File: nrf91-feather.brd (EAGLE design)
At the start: 50.8 x 22.9 mm, 126 parts, among them J1 CON-USB-1050170001, J2 CON-HEADER-1X12-MALE-PIN, J3 CON-HEADER-1X16-MALE-PIN, J4 CON-1909763-1, J5 CON-SIM-104224-0820, J6 CON-S2B-PH-SM4-TB(LF)(SN), J7 CON-1909763-1, J9 CON-TC2030-MCP-NL, Q1 MOSFET-P-SC89, Q2 MOSFET-DUAL-COMP-SOT563, Q3 MOSFET-P-20V-4.7A-SOT23, Q4 MOSFET-N-SC89, Q5 MOSFET-N-SC89, SW1 SW-EVP-AA402W, SW2 SW-EVP-AA402W, U1 MOD-NRF9160-SICA-R, U10 IC-LIS2DH12TR, U2 IC-CP2102N-A02-GQFN20R, U3 IC-TPS63031DSKR, U5 IC-TPD4S012DRYR, U6 FLASH-W25Q32JVZPIQ-WSON, U7 IC-STBC08PMR, U8 IC-PCF85063ATL/1, U9 IC-BAV70S, Y1 XTAL-ABS07AIG-32.768KHZ-7-T

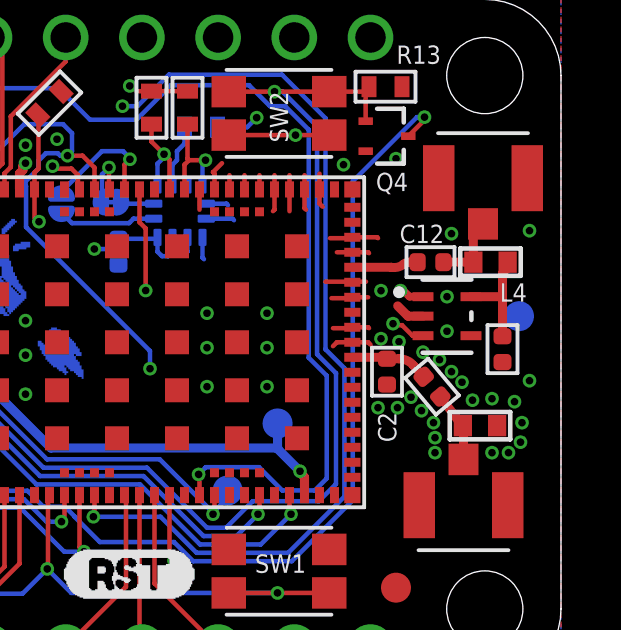
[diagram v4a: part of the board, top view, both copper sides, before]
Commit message: Undo changing U4 to LDO. Needs to stay as a load switch.
Changed:
* U4 back to the original part.
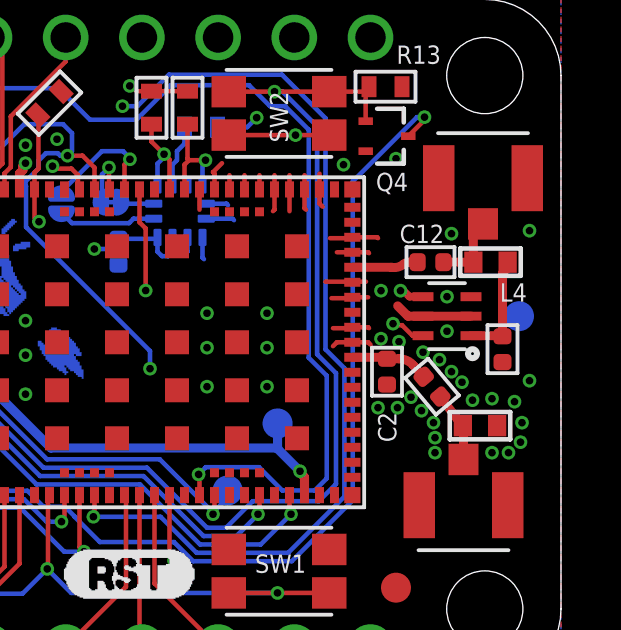
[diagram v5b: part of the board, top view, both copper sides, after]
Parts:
- U4: value (none) -> POWER-SWITCH-MIC94092YC6; device wolff-den:SOT353 -> wolff-den:SOT363
- turned U4 to 90 degrees
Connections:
- net +3V3: now also U4.4; no longer U4.1
- net COEX0/LNA_EN: now also U4.6; no longer U4.3
- net GND: now also U4.5
- net LNA_SW_OUT: now also U4.1; no longer U4.5
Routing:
- net GND: track 47.1 -> 48.7 mm
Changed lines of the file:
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@@
 <layer number="49" name="Reference" color="7" fill="1" visible="no" active="yes"/>
 <layer number="50" name="dxf" color="7" fill="1" visible="no" active="no"/>
-<layer number="51" name="tDocu" color="7" fill="1" visible="yes" active="yes"/>
+<layer number="51" name="tDocu" color="7" fill="1" visible="no" active="yes"/>
 <layer number="52" name="bDocu" color="7" fill="1" visible="no" active="yes"/>
 <layer number="53" name="tGND_GNDA" color="7" fill="9" visible="no" active="no"/>
@@
 <attribute name="TOLERANCE" value="5%" x="5.8" y="5.9" size="1.778" layer="27" display="off"/>
 </element>
-<element name="U4" library="wolff-den" library_urn="urn:adsk.eagle:library:6370453" package="SOT353" package3d_urn="urn:adsk.eagle:package:19061981/1" value="" x="47" y="12.3" smashed="yes">
-<attribute name="DESC" value="IC REG LINEAR 2.8V 150MA SC70-5" x="47" y="12.3" size="1.778" layer="27" display="off"/>
-<attribute name="DIGIKEYPN" value="576-3187-1-ND" x="47" y="12.3" size="1.778" layer="27" display="off"/>
-<attribute name="MPN" value="MIC5365-2.8YC5-TR" x="47" y="12.3" size="1.778" layer="27" display="off"/>
-<attribute name="NAME" x="45.0965" y="11.89428125" size="0.6096" layer="25" font="vector" ratio="20" rot="R90"/>
-<attribute name="NAME" x="47" y="12.3" size="0.2" layer="51" align="center"/>
+<element name="U4" library="wolff-den" library_urn="urn:adsk.eagle:library:6370453" package="SOT363" package3d_urn="urn:adsk.eagle:package:5807345/9" value="POWER-SWITCH-MIC94092YC6" x="47" y="12.3" smashed="yes" rot="R90">
+<attribute name="DESC" value="IC LOAD SW HGH SIDE 1.2A SC70-6" x="47" y="12.3" size="1.778" layer="27" rot="R90" display="off"/>
+<attribute name="DIGIKEYPN" value="576-3488-1-ND" x="47" y="12.3" size="1.778" layer="27" rot="R90" display="off"/>
+<attribute name="MPN" value="MIC94092YC6-TR" x="47" y="12.3" size="1.778" layer="27" rot="R90" display="off"/>
+<attribute name="NAME" x="44.5035" y="12.95571875" size="0.6096" layer="25" font="vector" ratio="20" rot="R270"/>
+<attribute name="NAME" x="47" y="12.3" size="0.2" layer="51" rot="R90" align="center"/>
 </element>
 <element name="C2" library="wolff-den" library_urn="urn:adsk.eagle:library:6370453" package="CAPC1005X55N" package3d_urn="urn:adsk.eagle:package:7419912/5" value="15p" x="45" y="10.45" smashed="yes" rot="R270">
@@
 <wire x1="44.85" y1="13.15" x2="44.8" y2="13.15" width="0.3" layer="1"/>
 <wire x1="45.69950625" y1="12.3" x2="45.35510625" y2="12.6444" width="0.3" layer="1"/>
-<wire x1="46.2" y1="12.3" x2="45.69950625" y2="12.3" width="0.3" layer="1"/>
+<wire x1="47.8" y1="12.3" x2="45.69950625" y2="12.3" width="0.3" layer="1"/>
 <contactref element="U10" pad="7"/>
 <contactref element="U10" pad="6"/>
@@
 <via x="11.8" y="4.45" extent="1-16" drill="0.254"/>
 <via x="12.85" y="4.85" extent="1-16" drill="0.254"/>
+<contactref element="U4" pad="5"/>
 </signal>
 <signal name="+3V3">
@@
 <wire x1="36.45" y1="20" x2="36.425" y2="19.975" width="0.1524" layer="1"/>
 <via x="36.425" y="19.975" extent="1-16" drill="0.254"/>
-<contactref element="U4" pad="1"/>
+<contactref element="U4" pad="4"/>
 <wire x1="45.45" y1="13.15" x2="45.55" y2="13.15" width="0.254" layer="1"/>
 <wire x1="45.75" y1="12.95" x2="45.55" y2="13.15" width="0.254" layer="1"/>
@@
 <wire x1="33.4" y1="15.45" x2="33.8794" y2="14.9706" width="0.1524" layer="2"/>
 <contactref element="R1" pad="2"/>
-<contactref element="U4" pad="3"/>
+<contactref element="U4" pad="6"/>
 <wire x1="46.2" y1="11.65" x2="45.85" y2="11.65" width="0.1524" layer="1"/>
 <wire x1="45.2" y1="12.05" x2="45.1842" y2="12.05" width="0.1524" layer="2"/>
@@
 <contactref element="L4" pad="1"/>
 <contactref element="C19" pad="1"/>
-<contactref element="U4" pad="5"/>
+<contactref element="U4" pad="1"/>
 <wire x1="49.11075" y1="14.01075" x2="49.11075" y2="13.98925" width="0.254" layer="1"/>
-<wire x1="48.85" y1="11.63" x2="48.83" y2="11.65" width="0.3" layer="1"/>
 <wire x1="49.11075" y1="13.98925" x2="48.85" y2="13.7285" width="0.3" layer="1"/>
-<wire x1="48.85" y1="11.63" x2="48.85" y2="12.95" width="0.3" layer="1"/>
-<wire x1="48.85" y1="12.95" x2="48.85" y2="13.7285" width="0.3" layer="1"/>
+<wire x1="48.85" y1="11.63" x2="48.85" y2="13.7285" width="0.3" layer="1"/>
 <wire x1="49.0215" y1="14.1" x2="49.11075" y2="14.01075" width="0.3" layer="1"/>
-<wire x1="47.8" y1="12.95" x2="48.85" y2="12.95" width="0.3" layer="1"/>
+<wire x1="47.8" y1="11.65" x2="48.83" y2="11.65" width="0.3" layer="1"/>
+<wire x1="48.83" y1="11.65" x2="48.85" y2="11.63" width="0.3" layer="1"/>
 </signal>
 <signal name="GPS_ANT" class="2">

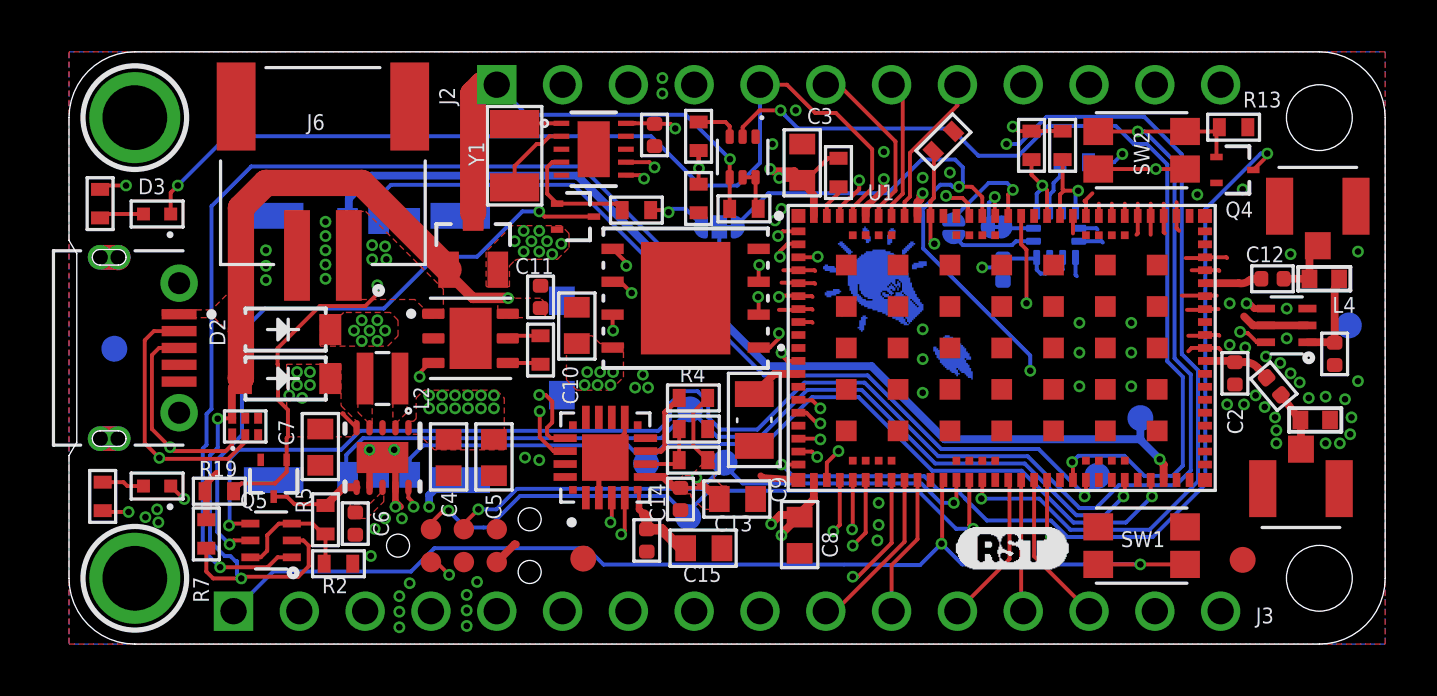
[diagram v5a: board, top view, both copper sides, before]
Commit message: Changes for next revision of the nRF9160 Feather
Removed:
* TVS diode

Changed:
* USB is now USB-C
* Power supply is now Boost + LDO combo (not final)
* LED position due to USB-C being larger
* Changed Schottky diodes to a TSC part
* Re-routed and cleaned up some signals on the inner layer
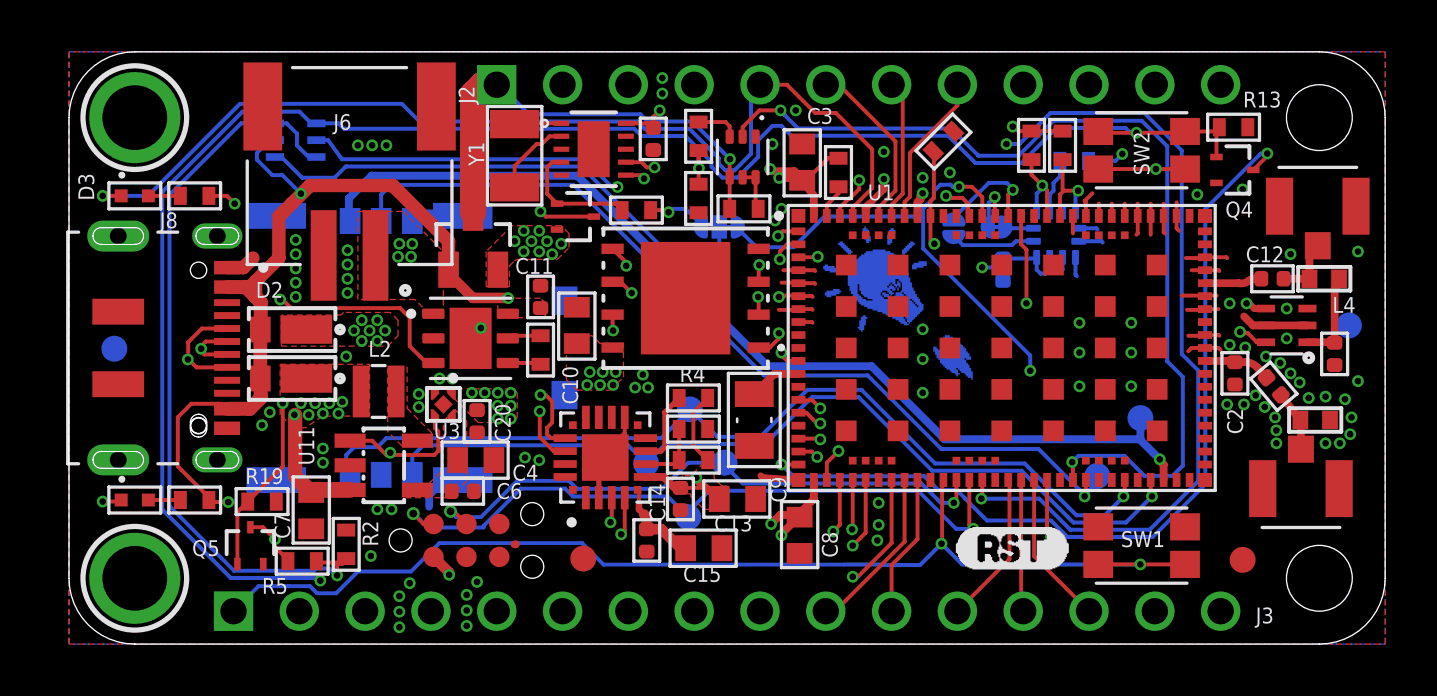
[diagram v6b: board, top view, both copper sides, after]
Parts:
- removed C5: 10u, wolff-den:C0603
- removed J1: CON-USB-1050170001, wolff-den:MOLEX_1050170001-NO-PAD
- removed R7: 100k, wolff-den:R0402-M
- removed U5: IC-TPD4S012DRYR, wolff-den:PSON50P100X145X50-6N
- added C20: 1u, wolff-den:CAPC1005X55N
- added J8: CON-USB-DX07S016JA1R1500, wolff-den:JAE_DX07S016JA1R1500
- added U11: POWER-VREG-EN-SW-500MA, wolff-den:SOT25
- C6: value 0.1u -> 1u
- D1, D2: value DIO-SCHOTTKY-3A-01 -> DIO-SCHOTTKY-1A-SMA-MICRO; device wolff-den:SOD123 -> wolff-den:SMA-MICRO
- R14: value 330 -> 1k
- U3: value IC-TPS63031DSKR -> (none); device wolff-den:DSK0010A -> wolff-den:DFN4
- moved SOLDER1 245.9 mm to (-173.7, -118.9)
- moved PCB1 196.2 mm to (-172.4, -119.4)
- moved U9 15.5 mm to (8.75, 19.4), flipped to the bottom
- moved C6 4.33 mm to (15.2, 5.90), turned to 0 degrees
- moved R11 3.66 mm to (4.85, 17.3), turned to 0 degrees
- moved R14 3.55 mm to (4.85, 5.56), turned to 0 degrees
- moved U3 3.12 mm to (14.4, 9.25)
- moved Q5 2.75 mm to (7.00, 3.80), turned to 0 degrees
- moved C7 2.47 mm to (9.35, 5.15)
- moved R5 1.84 mm to (9.00, 3.20), turned to 0 degrees
- moved R19 1.70 mm to (7.45, 5.50), turned to 180 degrees
- moved D3 1.11 mm to (2.54, 17.3), turned to 180 degrees
- moved C4 1.05 mm to (15.7, 7.10), turned to 0 degrees
- moved J6 1.03 mm to (10.8, 15.0)
- moved D4 1.02 mm to (2.54, 5.56), turned to 180 degrees
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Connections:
- removed net N$1: L2.P$1, U3.4
- removed net N$14: C6.1, U3.8
- new net N$15: C4.1, C6.1, U11.4, U3.4
- net +3V3: now also C20.1; no longer C4.1, C5.1, R14.2, U3.10
- net DIFF_N: now also J8.5, J8.8; no longer J1.2, U5.2
- net DIFF_P: now also J8.6, J8.7; no longer J1.3, U5.1
- net GND: now also C20.2, J8.1, J8.12, J8.S1, J8.S2, J8.S3, J8.S4, J8.S5, J8.S6, U11.2, U3.2; no longer C5.2, J1.5, J1.SH1, J1.SH10, J1.SH2, J1.SH3, J1.SH8, J1.SH9, R7.1, U3.11, U3.3, U3.7, U3.9, U5.4
- net N$2: now also U11.5; no longer U3.2
- net PS_EN: now also U11.1, U3.3; no longer U3.6
- net VBUS: now also J8.11, J8.2, R14.2; no longer J1.1, R7.2, U5.6
- net VSYS: now also L2.P$1, U11.3; no longer U3.5
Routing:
- net PS_EN_CC: track 5.36 -> 29.4 mm, vias 0 -> 1
- net NRF_PS_EN_JMP: track 39.6 -> 19.8 mm, vias 1 -> 0
- net PS_EN: track 3.73 -> 13.3 mm, vias 0 -> 2
- net RTC_PS_EN: track 25.3 -> 17.9 mm
- net CHRG: track 12.7 -> 19.3 mm
- net GND: track 48.7 -> 42.9 mm, vias 85 -> 91
- net DIFF_N: track 30.6 -> 25.7 mm
- net VSYS: track 54.0 -> 58.5 mm, vias 18 -> 20
- net DIFF_P: track 27.1 -> 22.8 mm
- net P0.03/D7: track 36.9 -> 39.7 mm
- net MODE/WAKE: track 72.9 -> 70.2 mm
- net P0.31/NRF_PS_EN: track 35.3 -> 32.7 mm
- net SWCLK: track 21.7 -> 23.4 mm
- net +3V3: track 22.5 -> 20.9 mm, vias 31 -> 25
- net VBUS: track 53.7 -> 52.2 mm
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- added copper zone on layer 1, net N$15
- removed copper zone on layer 1, net N$1
- removed copper zone on layer 1, net N$14
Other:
- outline, holes or cut-outs redrawn
- board text added: "BRD-0015-04"
- board text removed: "BRD-0015-03"

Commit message: Changed up power supply as the Torex part will not work. :(
Changed:
* Power supply to LM3281
* Cleaned up solder mask/paste mask for USB
* Removed paste mask for jumper

Added:
* Connection for enable pin to P0.13
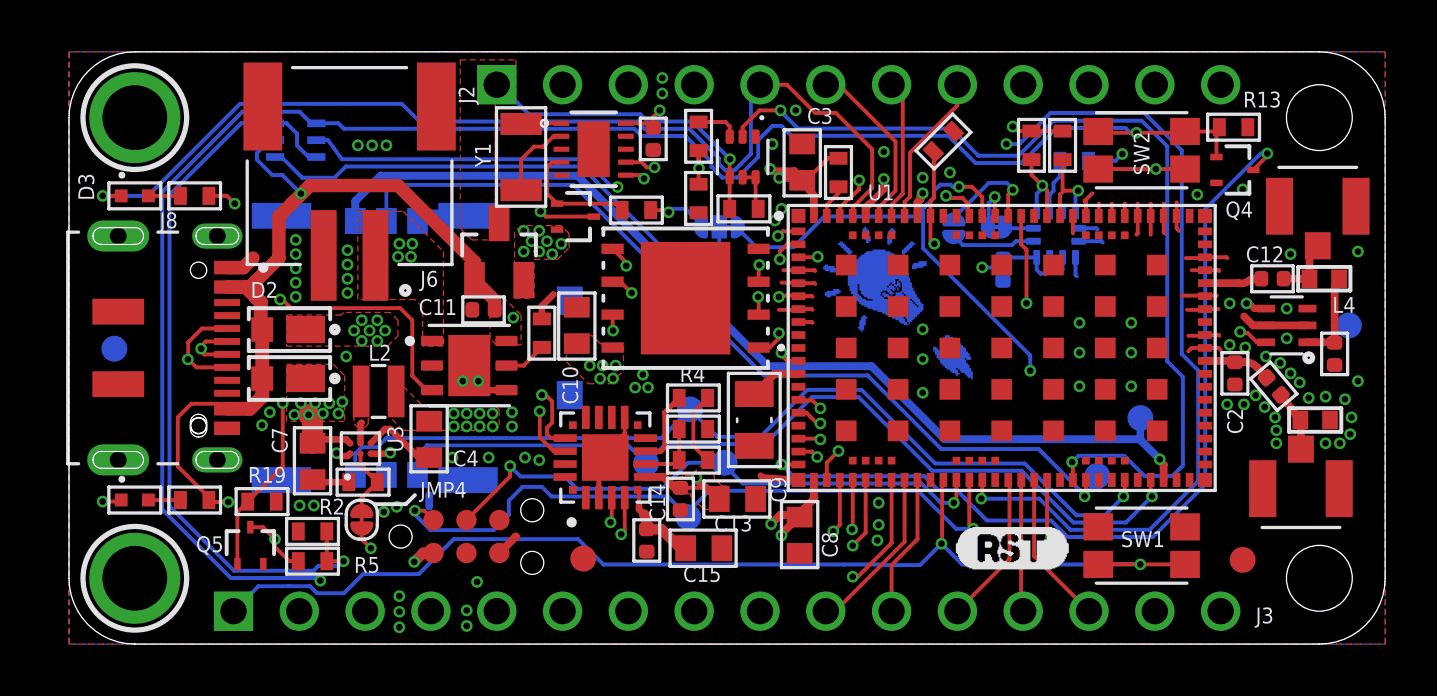
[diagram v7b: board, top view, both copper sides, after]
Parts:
- removed C20, C6: 1u, wolff-den:CAPC1005X55N
- removed U11: POWER-VREG-EN-SW-500MA, wolff-den:SOT25
- added JMP4: JUMPER-NC, wolff-den:JUMPER-ROUND-NC
- added R7: 1M, wolff-den:R0402-M
- C4, C7: value 10u -> 2.2u
- U3: value (none) -> IC-LM3281YFQR; device wolff-den:DFN4 -> wolff-den:BGA6N40P2X3_116X143X67N
- moved U3 3.62 mm to (11.2, 7.55), turned to 90 degrees
- moved C11 2.26 mm to (16.0, 12.9), turned to 180 degrees
- moved C4 1.97 mm to (13.9, 7.90), turned to 270 degrees
- moved C7 1.90 mm to (9.40, 7.05)
- moved R2 1.39 mm to (9.40, 4.35), turned to 0 degrees
- moved Q3 1.08 mm to (16.6, 15.2)
- moved U7 1.05 mm to (15.4, 10.8)
- moved D1 0.80 mm to (7.56, 10.2)
- moved D2 0.80 mm to (7.56, 12.1)
- moved R12 0.65 mm to (18.2, 12.0), turned to 270 degrees
- moved R5 0.40 mm to (9.40, 3.20)
- moved Y1 0.25 mm to (17.4, 18.8)
- moved J5 0.20 mm to (6.70, 11.4)
- moved J9 0.15 mm to (12.8, 4.15)
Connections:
- removed net N$15: C4.1, C6.1, U11.4, U3.4
- removed net N$2: L2.P$2, U11.5
- new net PS_MODE: JMP4.P$2, R7.2, U3.B1
- new net PS_SW: L2.P$1, U3.B2
- net +3V3: now also C4.1, L2.P$2, U3.A1; no longer C20.1, U3.1
- net GND: now also R7.1, U3.C2; no longer C20.2, C6.2, U11.2, U3.2
- net P0.13/A0: now also JMP4.P$1
- net PS_EN: now also U3.C1; no longer U11.1, U3.3
- net VSYS: now also U3.A2; no longer L2.P$1, U11.3
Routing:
- net P0.13/A0: track 18.3 -> 25.1 mm, vias 1 -> 2
- net GND: track 42.9 -> 49.4 mm, vias 91 -> 89
- net VBAT: track 25.2 -> 19.5 mm
- net VSYS: track 58.5 -> 54.1 mm, vias 20 -> 19
- net PS_EN: track 13.3 -> 9.17 mm
- net PS_MODE: track 0.00 -> 2.77 mm
- net VBUS: track 52.2 -> 50.9 mm
- net SWCLK: track 23.4 -> 22.4 mm
- net CHRG: track 19.3 -> 20.2 mm
- net PS_SW: track 0.00 -> 0.82 mm
- net SIM_VCC: track 39.0 -> 38.4 mm
- added copper zone on layer 1, net PS_SW
- removed copper zone on layer 1, net N$15
- removed copper zone on layer 1, net N$2

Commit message: Latest changes to nRF91
Changed:
* Power supply inductor
* Power supply tests board updated
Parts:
- L2: value 1.5u -> 470nH; device wolff-den:IND-2P0X2P0X1P2 -> wolff-den:INDC2012X100N
- moved L2 0.50 mm to (11.9, 9.25)
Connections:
- net +3V3: now also L2.2; no longer L2.P$2
- net PS_SW: now also L2.1; no longer L2.P$1
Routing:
- net GND: track 49.4 -> 48.6 mm, vias 89 -> 94
- net VSYS: vias 19 -> 18
